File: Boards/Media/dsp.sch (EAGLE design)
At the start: 119 parts, among them IC2 OPA2277U, IC4 OPA2277U, IC5 OPA2277U, IC6 OPA2277U, IC7 OPA2277U, IC8 OPA2277U, Y1 12.288MHz

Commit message: DSP sch nearly complete, added most components. Still needs reset generator and final check
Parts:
- removed IC8: OPA2277U, linear:OPA2277U
- added C100, C62, C64, C65, C66, C67, C68, C70, C79, C80, C89, C90, C99: 0.1uF, 1_SparkFun-Capacitors:CAP0603-CAP
- added C101, C102, C104, C107, C108, C109, C110, C111, C112, C61, C63, C69, C71, C81, C82, C91, C92: 10u, rcl:CPOL-USB
- added C103, C105, C106, C72, C73, C83, C84, C93, C94: 10uF-A, 1_SparkFun-Capacitors:CAP_POLC
- added C113, C114: 12p, 1_SparkFun-Capacitors:CAP0603-CAP
- added C115, C116: .1u, 1_SparkFun-Capacitors:CAP0603-CAP
- added C74, C75, C85, C86, C95, C96: 1n, 1_SparkFun-Capacitors:CAP0603-CAP
- added C76, C77, C78, C87, C88, C97, C98: 100p, 1_SparkFun-Capacitors:CAP0603-CAP
- added JP10: XLR Aux IN, 1_SparkFun-Connectors:M03POLAR
- added JP11: DVD In, 1_SparkFun-Connectors:M02POLAR
- added JP12: PC Input Stereo, 1_SparkFun-Connectors:M03POLAR
- added JP13: USB Audio, 1_SparkFun-Connectors:M04POLAR
- added JP14: RPi Audio In, 1_SparkFun-Connectors:M04POLAR
- added R26, R27, R28, R29, R30, R31, R32, R33: (no value), 1_SparkFun-Resistors:RESISTOR1206
- added R34, R35, R36, R37, R42, R43, R48, R49: 200, 1_SparkFun-Resistors:RESISTOR1206
- added R38, R39, R40, R41, R44, R45, R46, R47, R50, R51, R52, R53, R54, R55, R56: 4.7K, 1_SparkFun-Resistors:RESISTOR1206
- added R57, R61: 1M, 1_SparkFun-Resistors:RESISTOR1206
- added R58, R59: 22, 1_SparkFun-Resistors:RESISTOR1206
- added R60: 1.5K, 1_SparkFun-Resistors:RESISTOR1206
- added TP4: VOUT-L, 1_SparkFun-Passives:TEST-POINT3
- added TP5: VOUT-R, 1_SparkFun-Passives:TEST-POINT3
- added TP6: VIN-L, 1_SparkFun-Passives:TEST-POINT3
- added TP7: VIN-R, 1_SparkFun-Passives:TEST-POINT3
- added TP8: Suspend, 1_SparkFun-Passives:TEST-POINT3
- added U$35, U$38, U$39: LME49724, 0_DSP:LME49724
- added U$40: PCM2903, 0_DSP:PCM2903
- added U$43: 74AHC1G08, 1_SparkFun-DigitalIC:74AHC1G08
- added Y2: 12MHz, 1_SparkFun-FreqCtrl:CRYSTALHC49UV
- C12, C17, C18, C28, C32, C39, C40, C43, C51, C52, C53, C54: device 1_SparkFun-Capacitors:CAP_POLPTH2 -> rcl:CPOL-USB
- C29: value 100uF -> 10u; device 1_SparkFun-Capacitors:CAP_POLPTH1 -> rcl:CPOL-USB
- C45: value 10u -> 0.1uF; device 1_SparkFun-Capacitors:CAP_POLPTH2 -> 1_SparkFun-Capacitors:CAP0603-CAP
- C46, C47: value 220uF -> 10u; device 1_SparkFun-Capacitors:CAP_POLPTH1 -> rcl:CPOL-USB
- C57: value 10u -> 10uF-A; device 1_SparkFun-Capacitors:CAP_POLPTH2 -> 1_SparkFun-Capacitors:CAP_POLC
- C58: value 0.1uF -> 10uF-A; device 1_SparkFun-Capacitors:CAP0603-CAP -> 1_SparkFun-Capacitors:CAP_POLC
- C59: value 0.1uF -> 1n
- C60: value 10u -> 1n; device 1_SparkFun-Capacitors:CAP_POLPTH2 -> 1_SparkFun-Capacitors:CAP0603-CAP
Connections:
- new net N$100: R59.2, U$40.D-
- new net N$101: R55.1, R56.1
- new net N$102: JP13.2, R59.1
- new net N$103: R60.2, U$43.Y
- new net N$104: C113.2, R61.2, U$40.XTI, Y2.2
- new net N$105: TP8.1, U$40.SPND
- new net N$106: C114.2, R61.1, U$40.XTO, Y2.1
- new net N$107: C115.2, U$40.S/PDIFIN
- new net N$108: C116.2, U$40.S/PDIFOUT
- new net N$37: C73.+, R33.1, U$39.OUT-
- new net N$48: C72.+, R32.1, U$39.OUT+
- new net N$50: R24.1, R27.2, U$35.-
- new net N$51: R23.1, R28.1, U$38.+
- new net N$53: C67.1, U$39.CM
- new net N$54: C72.-, R34.2
- new net N$55: C73.-, R35.2
- new net N$56: C57.+, R36.2
- new net N$57: R30.2, R32.2, U$39.+
- new net N$58: JP10.3, R30.1
- new net N$59: JP10.1, R31.1
- new net N$60: R31.2, R33.2, U$39.-
- new net N$61: C75.2, C76.2, R35.1, U$17G$1.ADC1_L-
- new net N$62: C58.+, R37.2
- new net N$63: C74.1, C76.1, R34.1, U$17G$1.ADC1_L+
- new net N$64: C60.2, C77.2, R37.1, U$17G$1.ADC1_R-
- new net N$65: C59.1, C77.1, R36.1, U$17G$1.ADC1_R+
- new net N$66: C58.-, IC5A.OUT, R38.2
- new net N$67: C57.-, IC5B.OUT, R39.2, R41.2
- new net N$68: IC5A.-IN, R38.1, R39.1
- new net N$69: IC5B.-IN, R40.2, R41.1
- new net N$70: C106.-, JP11.1
- new net N$71: C83.+, R42.2
- new net N$72: C86.2, C87.2, R43.1, U$17G$1.ADC2_L-
- new net N$73: C85.1, C87.1, R42.1, U$17G$1.ADC2_L+
- new net N$74: C84.+, R43.2
- new net N$75: C83.-, IC6B.OUT, R45.2, R47.2
- new net N$76: C84.-, IC6A.OUT, R44.2
- new net N$77: IC6A.-IN, R44.1, R45.1
- new net N$78: IC6B.-IN, R46.2, R47.1
- new net N$79: C103.+, C88.1, R46.1
- new net N$80: C93.+, R48.2
- new net N$81: C96.2, C97.2, R49.1, U$17G$1.ADC2_1-
- new net N$82: C95.1, C97.1, R48.1
- new net N$83: C94.+, R49.2
- new net N$84: C93.-, IC7B.OUT, R51.2, R53.2
- new net N$85: C94.-, IC7A.OUT, R50.2
- new net N$86: IC7A.-IN, R50.1, R51.1
- new net N$87: IC7B.-IN, R52.2, R53.1
- new net N$88: C105.+, C98.1, R52.1
- new net N$89: C103.-, JP12.1
- new net N$90: U$17G$1.ADC2_R+
- new net N$91: C105.-, JP12.3
- new net N$92: C106.+, C78.1, R40.1
- new net N$93: TP4.1, U$40.VOUTL
- new net N$94: TP5.1, U$40.VOUTR
- new net N$95: TP6.1, U$40.VINL
- new net N$96: TP7.1, U$40.VINR
- new net N$97: JP13.3, R58.1, R60.1
- new net N$98: R58.2, U$40.D+
- new net N$99: R54.2, R55.2, U$43.B
- new net VBUS: JP13.4, R54.1, R57.2, U$40.SEL1
- net 3.3V_A: now also C104.+, C18.+; no longer C39.+, C45.+
- net 3V3_D: now also C107.+, C108.+, C109.+, C110.+, C111.+, C112.+, C17.+, C40.+, C45.2, U$40.SEL0, U$40.VBUS, U$40.VCCC, U$40.VCCP1, U$40.VCCP2, U$40.VCCX, U$40.VCOM, U$40.VDD, U$43.A, U$43.VCC; no longer C12.+, C32.+
- net BCLK2: now also U$17G$1.BCLKOUT
- net BCLK3: now also JP14.1
- net BCLK_OUT1: now also U$17G$3.BCLKIN
- net CLOCK: now also U$17G$2.MCLK-IN
- net DATA2: now also U$17G$1.DATAOUT0
- net DATA3: now also JP14.3
- net DATA_OUT1: now also U$17G$3.DATAIN0
- net FILTER: now also C39.+; no longer C40.+
- net GND: now also C100.2, C101.-, C102.-, C104.-, C107.-, C108.-, C109.-, C110.-, C111.-, C112.-, C113.1, C114.1, C29.-, C45.1, C47.-, C51.+, C59.2, C60.1, C61.-, C62.1, C63.+, C64.1, C65.2, C66.2, C67.2, C68.2, C69.-, C70.2, C71.+, C74.2, C75.1, C78.2, C79.1, C80.2, C81.+, C82.+, C85.2, C86.1, C88.2, C89.1, C90.2, C91.+, C92.-, C95.2, C96.1, C98.2, C99.1, IC5A.+IN, IC5B.+IN, IC6A.+IN, IC6B.+IN, IC7A.+IN, IC7B.+IN, JP10.2, JP11.2, JP12.2, JP13.1, JP14.4, R56.2, R57.1, U$35.E, U$38.E, U$39.E, U$40.AGNDC, U$40.AGNDP, U$40.AGNDX, U$40.DGND, U$40.DGNDU, U$43.GND; no longer C29.+, C45.-, C47.+, C51.-, C57.-, C58.2, C59.1, C60.+
- net LRCLK2: now also U$17G$1.LRLCKOUT
- net LRCLK3: now also JP14.2
- net LRCLK_OUT1: now also U$17G$3.LRCLKIN
- net N$17: now also C29.+; no longer C29.-
- net N$38: now also JP9.1, R28.2, U$38.OUT+; no longer IC6A.+IN, U$17G$3.DAC2_R+
- net N$39: now also JP9.3, R29.2, U$38.OUT-; no longer IC6B.+IN, U$17G$3.DAC2_R-
- net N$4: now also C12.+; no longer C18.+
- net N$40: now also JP8.1, R26.1, U$35.OUT+; no longer IC5A.+IN, U$17G$3.DAC2_L+
- net N$41: now also JP8.3, R27.1, U$35.OUT-; no longer IC5B.+IN, U$17G$3.DAC2_L-
- net N$42: now also R24.2, U$17G$3.DAC2_L-; no longer IC5A.-IN, IC5A.OUT, R22.1
- net N$43: now also C66.1, U$35.CM; no longer IC5B.-IN, IC5B.OUT, R23.1
- net N$44: now also C65.1, U$38.CM; no longer IC6A.-IN, IC6A.OUT, R24.1
- net N$45: now also R25.2, U$17G$3.DAC2_L+; no longer IC6B.-IN, IC6B.OUT, R25.1
- net N$46: now also R23.2, U$17G$3.DAC2_R+; no longer JP8.1, R22.2
- net N$47: now also R22.2, U$17G$3.DAC2_R-; no longer JP8.3, R23.2
- net N$49: now also R25.1, R26.2, U$35.+; no longer JP9.1, R24.2
- net N$52: now also R22.1, R29.1, U$38.-; no longer JP9.3, R25.2
- net N$7: now also C32.+; no longer C17.+
- net SPDIF-OUT: now also C115.1
- net SPDIFIN: now also C116.1
- net VCC: now also C101.+, C102.+, C47.+, C61.+, C62.2, C68.1, C69.+, C79.2, C89.2, C92.+, C99.2, U$35.V+, U$38.V+, U$39.V+; no longer C51.+, C57.+, C58.1, IC8P.V+
- net VNEG: now also C100.1, C51.-, C63.-, C64.2, C70.1, C71.-, C80.1, C81.-, C82.-, C90.1, C91.-, U$35.V-, U$38.V-, U$39.V-; no longer C47.-, C59.2, C60.-, IC8P.V-
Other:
- note added: "ADCs"
- note added: "Codec Control"
- note added: "Codec Power"
- note added: "DACs"
- note added: "DVD"
- note added: "Mic/Aux"
- note added: "PC 2"
- note added: "Reset"
- note removed: "ADC Control"
- note removed: "ADC Power"

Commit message: Began laying out DSP board
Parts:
- removed C108, C109, C111, C51, C61, C63, C69, C71, C91, C92: 10u, rcl:CPOL-USB
- removed JP2: (no value), 1_SparkFun-Connectors:M04PTH
- removed TP1: FM antenna, 1_SparkFun-Passives:TEST-POINT3
- added C117: 0.1u, 1_SparkFun-Capacitors:CAP0603-CAP
- added JP15: FM Antenna, 1_SparkFun-Connectors:M02PTH
- added R62: 10K, 1_SparkFun-Resistors:RESISTOR1206
- added S1: (no value), 1_SparkFun-Electromechanical:TAC_SWITCHPTH
- added U$52: TLV803, 0_DSP:TLV803
- C47: value 10u -> 0.1uF; device rcl:CPOL-USB -> 1_SparkFun-Capacitors:CAP0603-CAP
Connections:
- removed net N$24: U$17G$4.AGND@1, U$17G$4.AGND@2, U$17G$4.AGND@3, U$17G$4.AGND@4, U$17G$4.AGND@5, U$17G$4.DGND@1, U$17G$4.DGND@2, U$17G$4.VDRIVE, U$17G$4.VSENSE, U$17G$4.VSUPP
- net !RESET: now also R62.1, S1.1, S1.2, U$52.!RST
- net 3V3_D: now also C117.2, C47.2, R62.2, U$52.VCC; no longer C108.+, C109.+, C111.+
- net FM: now also JP15.2; no longer TP1.1
- net GND: now also C117.1, C47.1, JP15.1, S1.3, S1.4, U$17G$4.AGND@1, U$17G$4.AGND@2, U$17G$4.AGND@3, U$17G$4.AGND@4, U$17G$4.AGND@5, U$17G$4.DGND@1, U$17G$4.DGND@2, U$17G$4.VDRIVE, U$17G$4.VSENSE, U$17G$4.VSUPP, U$52.GND; no longer C108.-, C109.-, C111.-, C47.-, C51.+, C61.-, C63.+, C69.-, C71.+, C91.+, C92.-
- net N$102: now also JP13.3; no longer JP13.2
- net N$11: no longer JP2.1
- net N$14: no longer JP2.2
- net N$15: no longer JP2.3
- net N$16: no longer JP2.4
- net N$97: now also JP13.2; no longer JP13.3
- net VCC: no longer C47.+, C61.+, C69.+, C92.+
- net VNEG: no longer C51.-, C63.-, C71.-, C91.-
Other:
- note added: "PI/Aux"
- note added: "Power Supervisor"
- note removed: "Reset Circuitry!!!"

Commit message: DSP Board finished!
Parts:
- added LED1, LED2, LED3, LED4: (no value), 1_SparkFun-LED:LED1206
- added R63, R64: 1K, 1_SparkFun-Resistors:RESISTOR1206
- added R65, R66: 160, 1_SparkFun-Resistors:RESISTOR1206
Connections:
- removed net N$90: U$17G$1.ADC2_R+
- new net N$110: LED3.A, R63.2
- new net N$111: LED4.A, R64.2
- new net N$112: LED1.A, R66.2
- new net N$113: LED2.A, R65.2
- net 3.3V_A: now also R65.1
- net 3V3_D: now also R66.1
- net GND: now also LED1.C, LED2.C, LED3.C, LED4.C
- net N$82: now also U$17G$1.ADC2_R+
- net VCC: now also R63.1
- net VNEG: now also R64.1
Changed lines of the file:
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@@
 <part name="GND52" library="1_SparkFun-Aesthetics" deviceset="GND" device=""/>
 <part name="JP15" library="1_SparkFun-Connectors" deviceset="M02" device="PTH" value="FM Antenna"/>
+<part name="LED1" library="1_SparkFun-LED" deviceset="LED" device="1206"/>
+<part name="LED2" library="1_SparkFun-LED" deviceset="LED" device="1206"/>
+<part name="LED3" library="1_SparkFun-LED" deviceset="LED" device="1206"/>
+<part name="LED4" library="1_SparkFun-LED" deviceset="LED" device="1206"/>
+<part name="R63" library="1_SparkFun-Resistors" deviceset="RESISTOR" device="1206" value="1K"/>
+<part name="R64" library="1_SparkFun-Resistors" deviceset="RESISTOR" device="1206" value="1K"/>
+<part name="R65" library="1_SparkFun-Resistors" deviceset="RESISTOR" device="1206" value="160"/>
+<part name="R66" library="1_SparkFun-Resistors" deviceset="RESISTOR" device="1206" value="160"/>
+<part name="GND74" library="1_SparkFun-Aesthetics" deviceset="GND" device=""/>
+<part name="GND76" library="1_SparkFun-Aesthetics" deviceset="GND" device=""/>
+<part name="GND119" library="1_SparkFun-Aesthetics" deviceset="GND" device=""/>
+<part name="GND121" library="1_SparkFun-Aesthetics" deviceset="GND" device=""/>
 </parts>
 <sheets>
@@
 <wire x1="10.16" y1="172.72" x2="83.82" y2="172.72" width="0.4064" layer="94"/>
 <wire x1="83.82" y1="172.72" x2="83.82" y2="185.42" width="0.4064" layer="94"/>
-<wire x1="83.82" y1="185.42" x2="152.4" y2="185.42" width="0.4064" layer="94"/>
-<wire x1="152.4" y1="185.42" x2="152.4" y2="251.46" width="0.4064" layer="94"/>
+<wire x1="83.82" y1="185.42" x2="175.26" y2="185.42" width="0.4064" layer="94"/>
+<wire x1="175.26" y1="185.42" x2="175.26" y2="251.46" width="0.4064" layer="94"/>
 <wire x1="7.62" y1="83.82" x2="109.22" y2="83.82" width="0.4064" layer="94"/>
 <wire x1="109.22" y1="83.82" x2="109.22" y2="88.9" width="0.4064" layer="94"/>
 <wire x1="109.22" y1="88.9" x2="195.58" y2="88.9" width="0.4064" layer="94"/>
 <wire x1="195.58" y1="88.9" x2="195.58" y2="185.42" width="0.4064" layer="94"/>
-<wire x1="195.58" y1="185.42" x2="152.4" y2="185.42" width="0.4064" layer="94"/>
+<wire x1="195.58" y1="185.42" x2="175.26" y2="185.42" width="0.4064" layer="94"/>
 <wire x1="195.58" y1="88.9" x2="195.58" y2="10.16" width="0.4064" layer="94"/>
 <text x="7.62" y="251.46" size="3.81" layer="94" ratio="14">Power Input</text>
@@
 <text x="12.7" y="12.7" size="3.81" layer="94" ratio="14">DSP Control</text>
 <text x="200.66" y="175.26" size="3.81" layer="94" ratio="14">Codec Power</text>
-<text x="162.56" y="243.84" size="3.81" layer="94" ratio="14">Codec Control</text>
+<text x="182.88" y="246.38" size="3.81" layer="94" ratio="14">Codec Control</text>
 <wire x1="195.58" y1="185.42" x2="378.46" y2="185.42" width="0.4064" layer="94"/>
 <text x="375.92" y="350.52" size="1.778" layer="91" rot="R90">Headphones</text>
@@
 <instance part="GND22" gate="1" x="119.38" y="226.06"/>
 <instance part="SUPPLY10" gate="G$2" x="81.28" y="200.66"/>
-<instance part="SUPPLY11" gate="1" x="81.28" y="213.36"/>
+<instance part="SUPPLY11" gate="1" x="81.28" y="218.44"/>
 <instance part="Y1" gate="G$1" x="35.56" y="66.04" rot="R90"/>
 <instance part="C25" gate="G$1" x="25.4" y="60.96" rot="R90"/>
@@
 <instance part="GND52" gate="1" x="177.8" y="337.82" rot="R270"/>
 <instance part="JP15" gate="G$1" x="167.64" y="297.18"/>
+<instance part="LED1" gate="G$1" x="157.48" y="236.22"/>
+<instance part="LED2" gate="G$1" x="157.48" y="208.28"/>
+<instance part="LED3" gate="G$1" x="93.98" y="215.9" rot="R90"/>
+<instance part="LED4" gate="G$1" x="93.98" y="205.74" rot="R90"/>
+<instance part="R63" gate="G$1" x="86.36" y="215.9"/>
+<instance part="R64" gate="G$1" x="86.36" y="205.74"/>
+<instance part="R65" gate="G$1" x="147.32" y="213.36"/>
+<instance part="R66" gate="G$1" x="147.32" y="241.3"/>
+<instance part="GND74" gate="1" x="101.6" y="215.9" rot="R90"/>
+<instance part="GND76" gate="1" x="101.6" y="205.74" rot="R90"/>
+<instance part="GND119" gate="1" x="157.48" y="198.12"/>
+<instance part="GND121" gate="1" x="157.48" y="226.06"/>
 </instances>
 <busses>
@@
 <pinref part="GND52" gate="1" pin="GND"/>
 </segment>
+<segment>
+<pinref part="LED3" gate="G$1" pin="C"/>
+<pinref part="GND74" gate="1" pin="GND"/>
+</segment>
+<segment>
+<pinref part="LED4" gate="G$1" pin="C"/>
+<pinref part="GND76" gate="1" pin="GND"/>
+</segment>
+<segment>
+<pinref part="LED1" gate="G$1" pin="C"/>
+<pinref part="GND121" gate="1" pin="GND"/>
+<wire x1="157.48" y1="231.14" x2="157.48" y2="228.6" width="0.1524" layer="91"/>
+</segment>
+<segment>
+<pinref part="LED2" gate="G$1" pin="C"/>
+<pinref part="GND119" gate="1" pin="GND"/>
+<wire x1="157.48" y1="203.2" x2="157.48" y2="200.66" width="0.1524" layer="91"/>
+</segment>
 </net>
 <net name="SCL" class="0">
@@
 <net name="VCC" class="0">
 <segment>
-<pinref part="JP1" gate="G$1" pin="3"/>
 <pinref part="SUPPLY11" gate="1" pin="VCC"/>
+<wire x1="81.28" y1="215.9" x2="81.28" y2="218.44" width="0.1524" layer="91"/>
+<pinref part="R63" gate="G$1" pin="1"/>
+<pinref part="JP1" gate="G$1" pin="3"/>
 <wire x1="30.48" y1="210.82" x2="58.42" y2="210.82" width="0.1524" layer="91"/>
-<wire x1="58.42" y1="210.82" x2="81.28" y2="210.82" width="0.1524" layer="91"/>
-<wire x1="81.28" y1="210.82" x2="81.28" y2="213.36" width="0.1524" layer="91"/>
 <pinref part="C1" gate="G$1" pin="+"/>
 <wire x1="58.42" y1="193.04" x2="58.42" y2="210.82" width="0.1524" layer="91"/>
+<wire x1="81.28" y1="215.9" x2="58.42" y2="215.9" width="0.1524" layer="91"/>
+<wire x1="58.42" y1="215.9" x2="58.42" y2="210.82" width="0.1524" layer="91"/>
 <junction x="58.42" y="210.82"/>
+<junction x="81.28" y="215.9"/>
 </segment>
 <segment>
@@
 <wire x1="81.28" y1="205.74" x2="73.66" y2="205.74" width="0.1524" layer="91"/>
 <pinref part="C2" gate="G$1" pin="-"/>
-<wire x1="71.12" y1="205.74" x2="30.48" y2="205.74" width="0.1524" layer="91"/>
-<wire x1="71.12" y1="205.74" x2="73.66" y2="205.74" width="0.1524" layer="91"/>
+<wire x1="73.66" y1="205.74" x2="30.48" y2="205.74" width="0.1524" layer="91"/>
 <wire x1="73.66" y1="205.74" x2="73.66" y2="193.04" width="0.1524" layer="91"/>
 <junction x="73.66" y="205.74"/>
+<pinref part="R64" gate="G$1" pin="1"/>
+<junction x="81.28" y="205.74"/>
 </segment>
 <segment>
@@
 <pinref part="U$2" gate="G$1" pin="3.3V_A"/>
 <junction x="137.16" y="213.36"/>
+<pinref part="R65" gate="G$1" pin="1"/>
+<wire x1="137.16" y1="213.36" x2="142.24" y2="213.36" width="0.1524" layer="91"/>
 </segment>
 <segment>
@@
 <pinref part="U$3" gate="G$1" pin="3V3_D"/>
 <junction x="137.16" y="241.3"/>
+<pinref part="R66" gate="G$1" pin="1"/>
+<wire x1="137.16" y1="241.3" x2="142.24" y2="241.3" width="0.1524" layer="91"/>
 </segment>
 <segment>
@@
 <wire x1="513.08" y1="304.8" x2="513.08" y2="312.42" width="0.1524" layer="91"/>
 <junction x="523.24" y="312.42"/>
-<wire x1="513.08" y1="312.42" x2="480.06" y2="312.42" width="0.1524" layer="91"/>
+<pinref part="U$17" gate="G$1" pin="ADC2_R+"/>
+<wire x1="469.9" y1="388.62" x2="474.98" y2="388.62" width="0.1524" layer="91"/>
+<wire x1="474.98" y1="388.62" x2="474.98" y2="312.42" width="0.1524" layer="91"/>
+<wire x1="474.98" y1="312.42" x2="513.08" y2="312.42" width="0.1524" layer="91"/>
 <junction x="513.08" y="312.42"/>
 </segment>
@@
 </segment>
 </net>
-<net name="N$90" class="0">
-<segment>
-<pinref part="U$17" gate="G$1" pin="ADC2_R+"/>
-<wire x1="469.9" y1="388.62" x2="474.98" y2="388.62" width="0.1524" layer="91"/>
-<wire x1="474.98" y1="388.62" x2="474.98" y2="312.42" width="0.1524" layer="91"/>
-<wire x1="474.98" y1="312.42" x2="480.06" y2="312.42" width="0.1524" layer="91"/>
-</segment>
-</net>
 <net name="N$91" class="0">
 <segment>
@@
 </segment>
 </net>
+<net name="N$110" class="0">
+<segment>
+<pinref part="LED3" gate="G$1" pin="A"/>
+<pinref part="R63" gate="G$1" pin="2"/>
+</segment>
+</net>
+<net name="N$111" class="0">
+<segment>
+<pinref part="LED4" gate="G$1" pin="A"/>
+<pinref part="R64" gate="G$1" pin="2"/>
+</segment>
+</net>
+<net name="N$112" class="0">
+<segment>
+<pinref part="R66" gate="G$1" pin="2"/>
+<pinref part="LED1" gate="G$1" pin="A"/>
+<wire x1="152.4" y1="241.3" x2="157.48" y2="241.3" width="0.1524" layer="91"/>
+<wire x1="157.48" y1="241.3" x2="157.48" y2="238.76" width="0.1524" layer="91"/>
+</segment>
+</net>
+<net name="N$113" class="0">
+<segment>
+<pinref part="R65" gate="G$1" pin="2"/>
+<pinref part="LED2" gate="G$1" pin="A"/>
+<wire x1="152.4" y1="213.36" x2="157.48" y2="213.36" width="0.1524" layer="91"/>
+<wire x1="157.48" y1="213.36" x2="157.48" y2="210.82" width="0.1524" layer="91"/>
+</segment>
+</net>

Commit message: Prepared board for production, last minute error checks and rotations
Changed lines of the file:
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@@
-</segment>
-</net>
-<net name="N$109" class="0">
-<segment>
-<wire x1="624.84" y1="515.62" x2="624.84" y2="477.52" width="0.1524" layer="91"/>
-<wire x1="624.84" y1="477.52" x2="635" y2="477.52" width="0.1524" layer="91"/>
-<wire x1="635" y1="477.52" x2="635" y2="434.34" width="0.1524" layer="91"/>
-<wire x1="635" y1="434.34" x2="650.24" y2="434.34" width="0.1524" layer="91"/>
-<wire x1="650.24" y1="434.34" x2="650.24" y2="398.78" width="0.1524" layer="91"/>
-<wire x1="650.24" y1="398.78" x2="749.3" y2="398.78" width="0.1524" layer="91"/>
 </segment>
 </net>

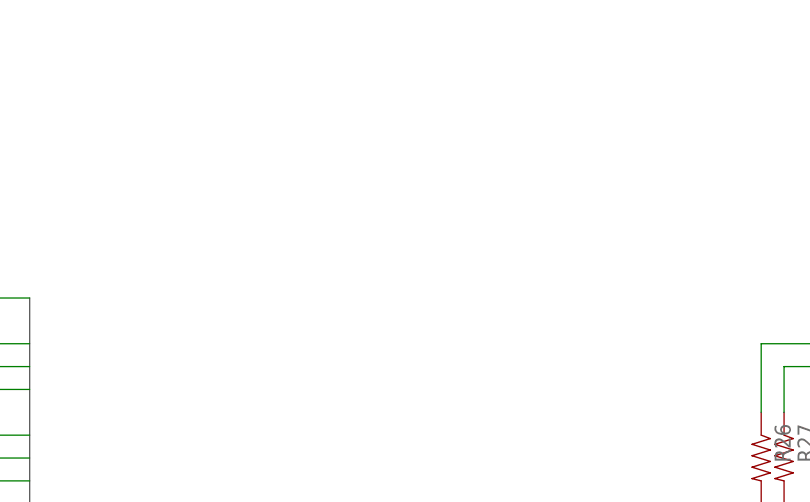
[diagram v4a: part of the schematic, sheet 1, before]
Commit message: Final gerbers and board updates! Fixed PCB violations, now passes FreeDFM check!
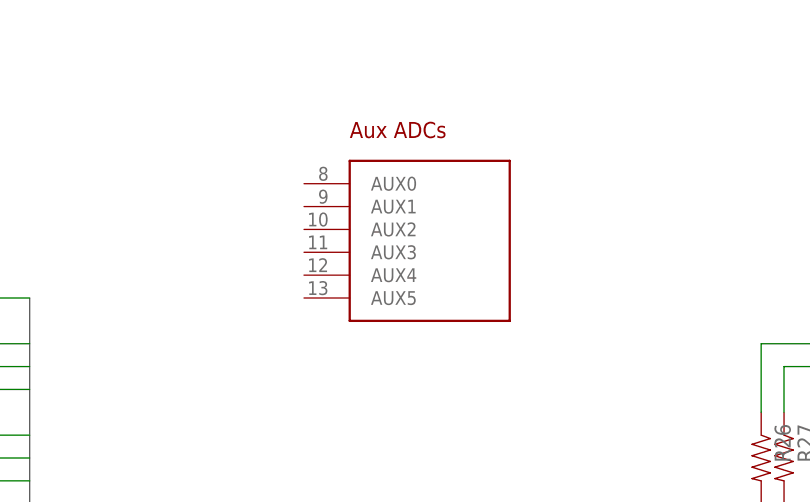
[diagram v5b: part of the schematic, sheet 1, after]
